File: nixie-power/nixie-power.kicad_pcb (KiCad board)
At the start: 2 copper layers, 49 x 49 mm, 22 parts, among them CON1 BARREL_JACK, P1 CONN_2, P2 CONN_2, P3 CONN_3, P4 CONN_1, P5 CONN_1, P6 CONN_1, P7 CONN_1, Q1 MOSFET_N, U1 MAX1771

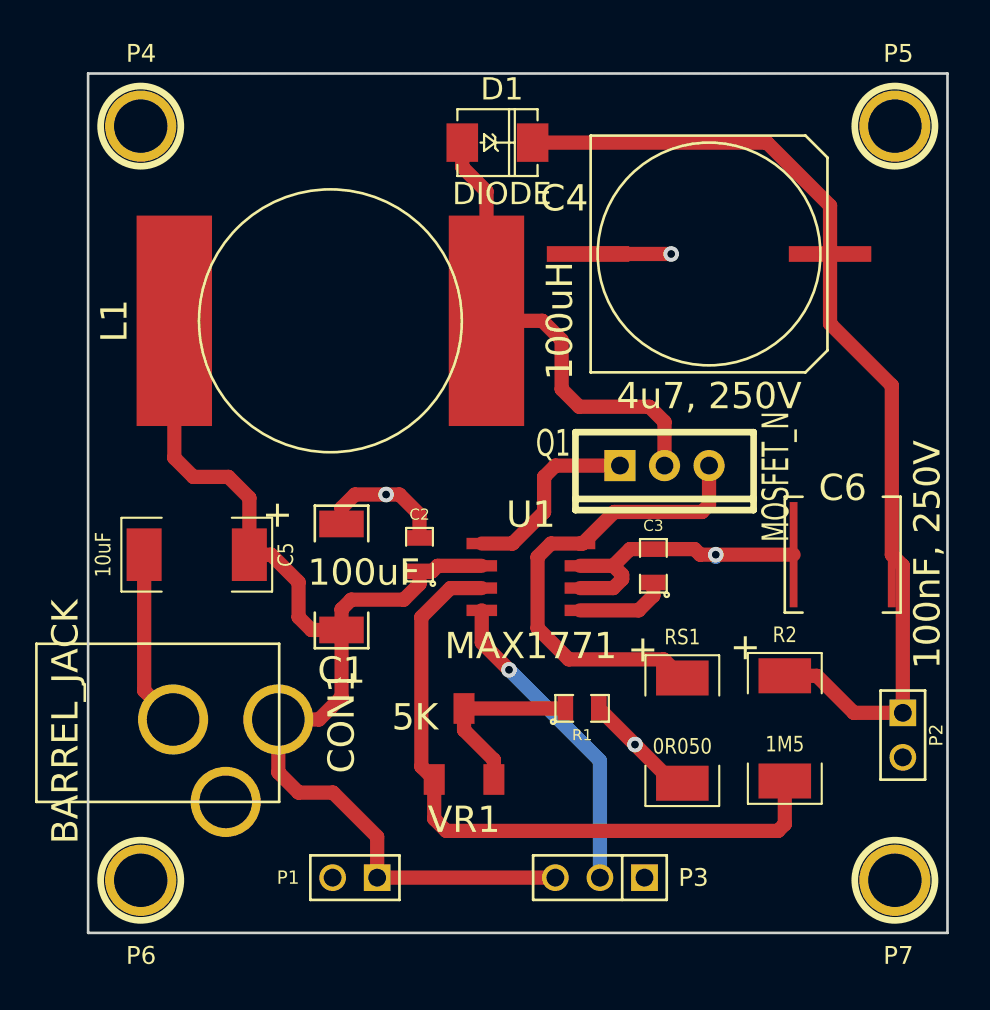
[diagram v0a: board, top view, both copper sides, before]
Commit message: nixie-power: Increase trace width.
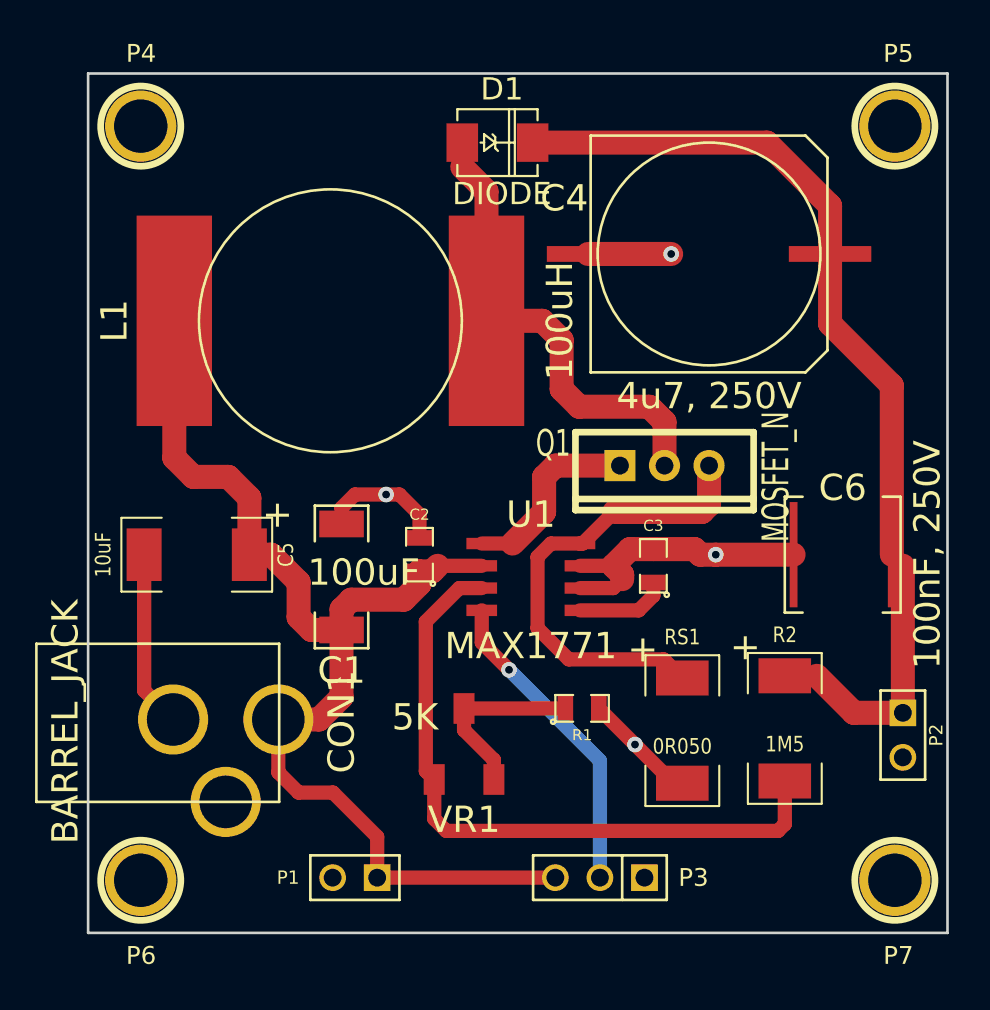
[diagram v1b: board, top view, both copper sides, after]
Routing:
- net FB: track 38.8 -> 38.3 mm

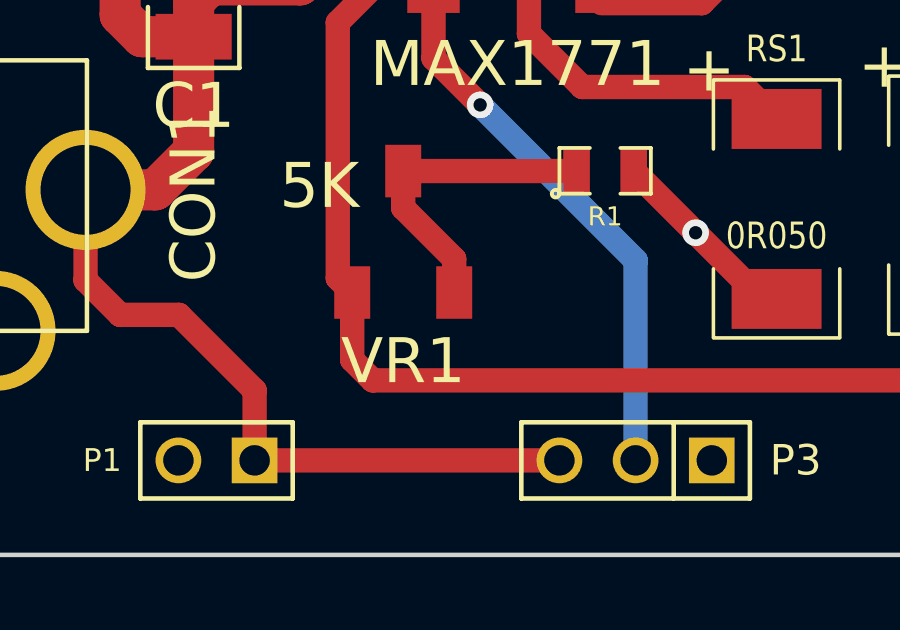
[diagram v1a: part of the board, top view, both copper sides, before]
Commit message: nixie-power: Add silk screen.
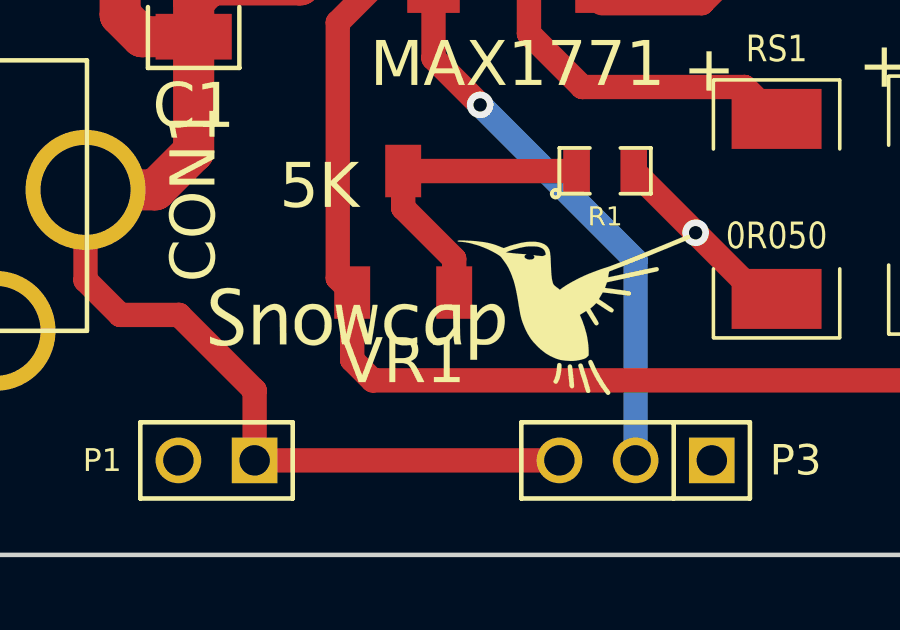
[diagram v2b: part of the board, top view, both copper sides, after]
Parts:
- added ?: , LOGO_SNOWCAP_FRONT, F.Cu at (53.0, 65.0)
- added ?: , LOGO_SNOWCAP_BACK, B.Cu at (53.0, 51.0)
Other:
- board text added: "NIXIE POWER v1"
